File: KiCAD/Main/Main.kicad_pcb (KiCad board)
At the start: 4 copper layers, 60 x 150 mm, 99 parts, among them J1 Micro_SD_Card_Det2, J2 Screw_Terminal_01x09, J3 Screw_Terminal_01x09, J4 USB_C_Receptacle_USB2.0_16P, J5 Conn_02x04_Counter_Clockwise, J8 Conn_Coaxial, J9 Conn_Coaxial, Q1 AO3400A, Q2 AO3400A, Q3 AO3400A, Q4 2N7002, SW1 RESET, SW2 USER, U1 LM2596S-3.3, U11 BMP390L, U12 BMP390L, U13 BMP390L, U14 BMI270, U15 BMI270, U16 BMI270, U17 SHT4x, U2 TPS2121RUXR, U3 LIS2MDL, U4 STM32H750VBTx, U5 MAX-M8Q, U7 ISM6HG256x, Y2 SiT8008xx-2x-xxE (25MHz)

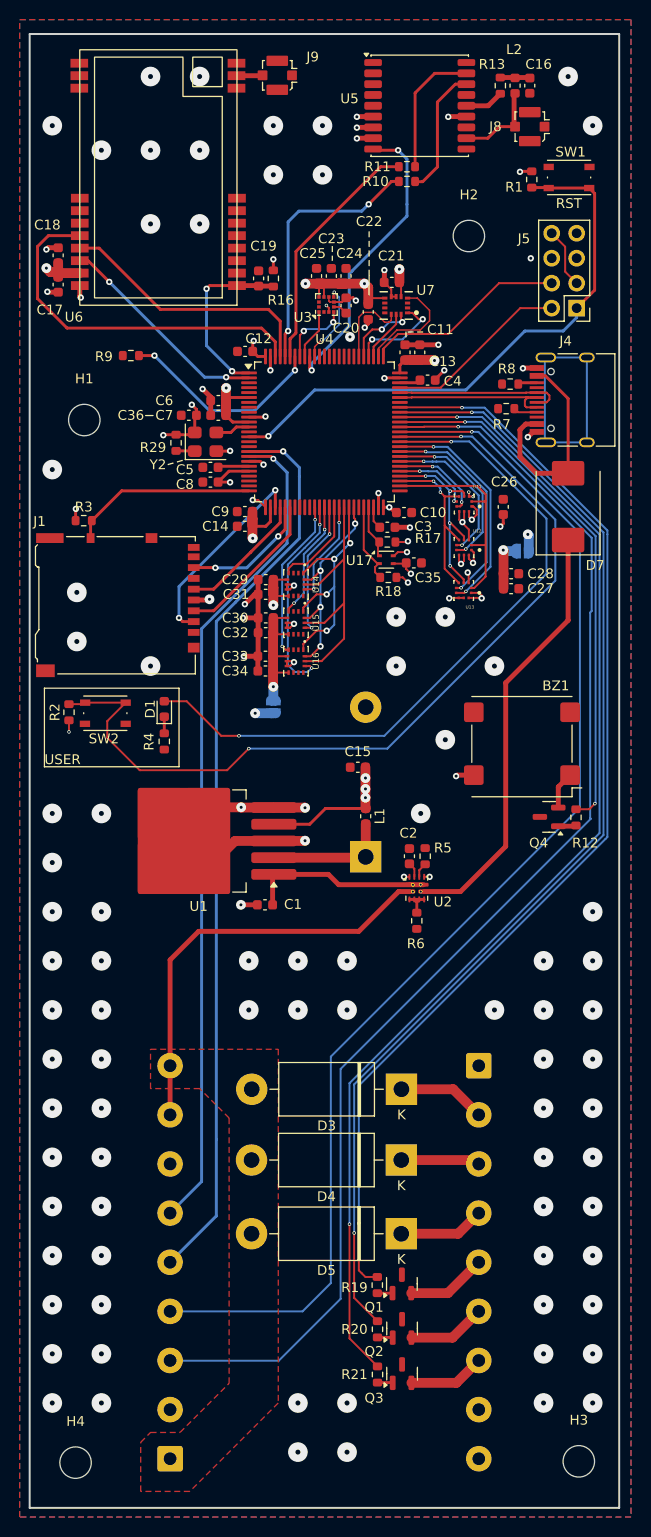
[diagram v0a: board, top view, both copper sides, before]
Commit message: Update aux magnetometer, test THs, and silkscreens
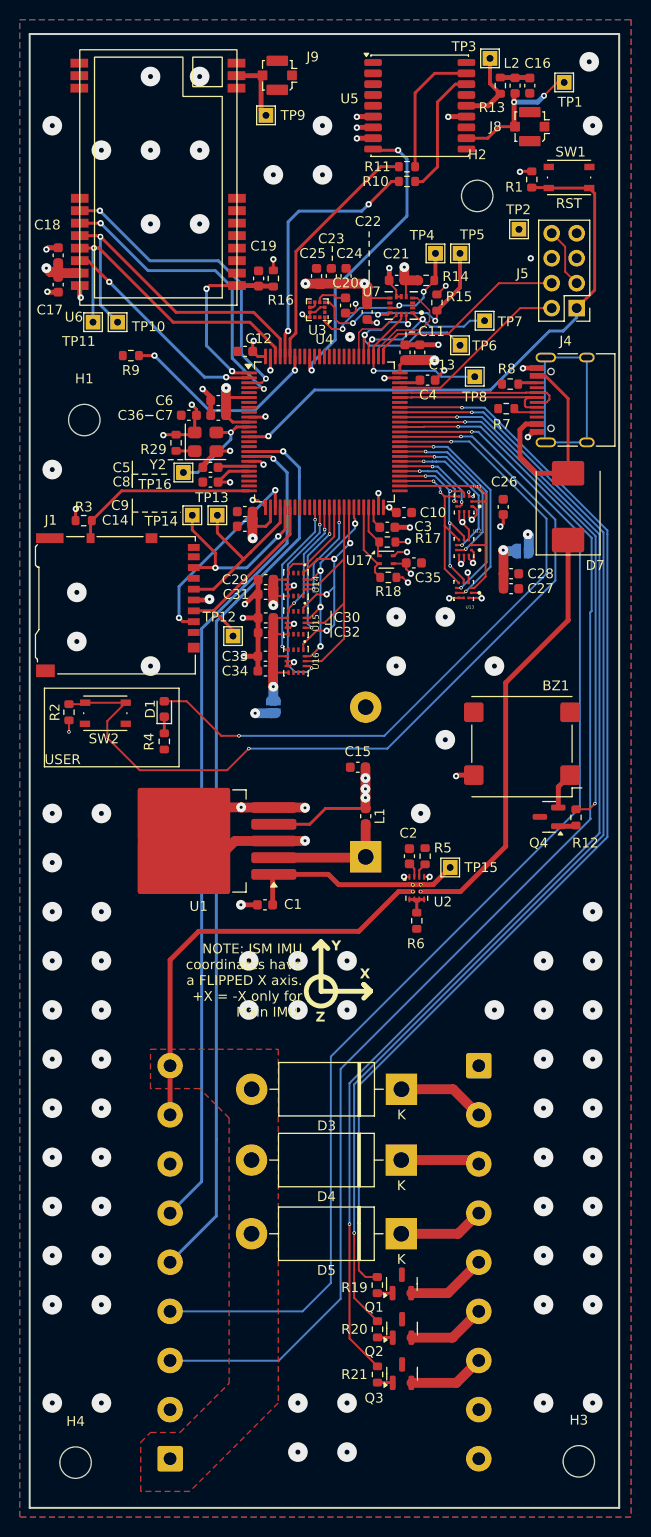
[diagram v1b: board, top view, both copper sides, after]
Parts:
- added R14: 10k, Resistor_SMD:R_0603_1608Metric, F.Cu at (148.1, 55.8)
- added R15: 10k, Resistor_SMD:R_0603_1608Metric, F.Cu at (149.2, 58.0)
- added TP1: TestPoint, TestPoint:TestPoint_THTPad_1.5x1.5mm_Drill0.7mm, F.Cu at (162.1, 35.6)
- added TP10: TestPoint, TestPoint:TestPoint_THTPad_1.5x1.5mm_Drill0.7mm, F.Cu at (116.7, 60.0)
- added TP11: TestPoint, TestPoint:TestPoint_THTPad_1.5x1.5mm_Drill0.7mm, F.Cu at (114.2, 60.0)
- added TP12: TestPoint, TestPoint:TestPoint_THTPad_1.5x1.5mm_Drill0.7mm, F.Cu at (128.4, 92.0)
- added TP13: TestPoint, TestPoint:TestPoint_THTPad_1.5x1.5mm_Drill0.7mm, F.Cu at (126.8, 79.7)
- added TP14: TestPoint, TestPoint:TestPoint_THTPad_1.5x1.5mm_Drill0.7mm, F.Cu at (124.2, 79.7)
- added TP15: TestPoint, TestPoint:TestPoint_THTPad_1.5x1.5mm_Drill0.7mm, F.Cu at (150.5, 115.5)
- added TP16: TestPoint, TestPoint:TestPoint_THTPad_1.5x1.5mm_Drill0.7mm, F.Cu at (123.3, 75.3)
- added TP2: TestPoint, TestPoint:TestPoint_THTPad_1.5x1.5mm_Drill0.7mm, F.Cu at (157.5, 50.5)
- added TP3: TestPoint, TestPoint:TestPoint_THTPad_1.5x1.5mm_Drill0.7mm, F.Cu at (154.6, 33.1)
- added TP4: TestPoint, TestPoint:TestPoint_THTPad_1.5x1.5mm_Drill0.7mm, F.Cu at (149.0, 53.0)
- added TP5: TestPoint, TestPoint:TestPoint_THTPad_1.5x1.5mm_Drill0.7mm, F.Cu at (151.5, 53.0)
- added TP6: TestPoint, TestPoint:TestPoint_THTPad_1.5x1.5mm_Drill0.7mm, F.Cu at (151.5, 62.4)
- added TP7: TestPoint, TestPoint:TestPoint_THTPad_1.5x1.5mm_Drill0.7mm, F.Cu at (154.0, 59.9)
- added TP8: TestPoint, TestPoint:TestPoint_THTPad_1.5x1.5mm_Drill0.7mm, F.Cu at (153.0, 65.5)
- added TP9: TestPoint, TestPoint:TestPoint_THTPad_1.5x1.5mm_Drill0.7mm, F.Cu at (131.8, 39.0)
- moved H2 4.17 mm to (153.2, 47.1)
- moved U3 1.07 mm to (137.0, 58.7), turned to 180 degrees
- moved C21 0.54 mm to (145.1, 55.7)
- moved U7 0.52 mm to (145.5, 58.3)
- moved C22 0.11 mm to (142.1, 59.0)
- moved C20 0.05 mm to (139.8, 58.3), turned to -90 degrees
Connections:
- U3 pad 1: /IMUs/SCL_LIS -> Net-(U3-SCL/SPC)
- U3 pad 4: /IMUs/SDA_LIS -> Net-(U3-SDA/SDI/SDO)
- U3 pad 7: /IMUs/INT_LIS -> unconnected-(U3-DRDY-Pad7)
- U4 pad 3: unconnected-(U4-PE4-Pad3) -> /Microcontroller/M0_Radio
- U4 pad 4: unconnected-(U4-PE5-Pad4) -> /Microcontroller/M1_Radio
- U4 pad 90: /IMUs/INT_LIS -> unconnected-(U4-PB4-Pad90)
- U4 pad 92: /IMUs/SCL_LIS -> unconnected-(U4-PB6-Pad92)
- U4 pad 93: /IMUs/SDA_LIS -> unconnected-(U4-PB7-Pad93)
- U4 pad 97: /Microcontroller/Radio RX -> /Microcontroller/Radio TX
- U4 pad 98: /Microcontroller/Radio TX -> /Microcontroller/Radio RX
- U6 pad 20: GND -> /Microcontroller/M0_Radio
- U6 pad 21: GND -> /Microcontroller/M1_Radio
- U7 pad 10: unconnected-(U7-OCS_Aux-Pad10) -> Net-(U3-SCL/SPC)
- U7 pad 11: unconnected-(U7-SDO_Aux-Pad11) -> Net-(U3-SDA/SDI/SDO)
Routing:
- net /Microcontroller/M0_Radio: track 0.00 -> 32.1 mm, vias 0 -> 2
- net /Microcontroller/M1_Radio: track 0.00 -> 31.5 mm, vias 0 -> 2
- net Net-(U3-SDA/SDI/SDO): track 0.00 -> 22.9 mm, vias 0 -> 3
- net Net-(U3-SCL/SPC): track 0.00 -> 18.7 mm, vias 0 -> 3
- net /IMUs/ISM_MOSI: track 7.33 -> 19.9 mm
- net /IMUs/ISM_SCK: track 5.24 -> 17.5 mm, vias 0 -> 1
- net /IMUs/INT_LIS: track 8.44 -> 0.00 mm, vias 2 -> 0
- net /IMUs/SDA_LIS: track 7.19 -> 0.00 mm, vias 2 -> 0
- net /Microcontroller/~{OSC_OUT}: track 3.56 -> 10.5 mm, vias 0 -> 1
- net /IMUs/ISM_MISO: track 9.69 -> 16.0 mm
- net /Microcontroller/SD_MISO: track 13.2 -> 19.5 mm
- net Net-(J8-In): track 8.91 -> 14.8 mm, vias 0 -> 2
- net /Microcontroller/Radio RX: track 27.1 -> 32.6 mm, vias 0 -> 1
- net /Microcontroller/SD_CLK: track 13.2 -> 18.4 mm
- net /IMUs/SCL_LIS: track 5.13 -> 0.00 mm
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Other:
- board text added: "9-Radio RF 10-Radio RX 11-Radio TX 12-SD MOSI 13-SD SCK 14-SD MISO 15-TPS Pwr-Out 16-MCU OSC-Out"
- board text added: "NOTE: ISM IMU coordinates have a FLIPPED X axis. +X = -X only for Main IMU."
- board text added: "Testing Point Legend 1-GPS RF 2-3V3 3-GPS VCC-RF 4-LIS SCL 5-LIS SDA 6-ISM MOSI 7-ISM MISO 8-ISM SCK"
- board text added: "X"
- board text added: "Y"
- board text added: "Z"

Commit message: Replace independent magnetometer, reformat test points, generate test gerber and BOM
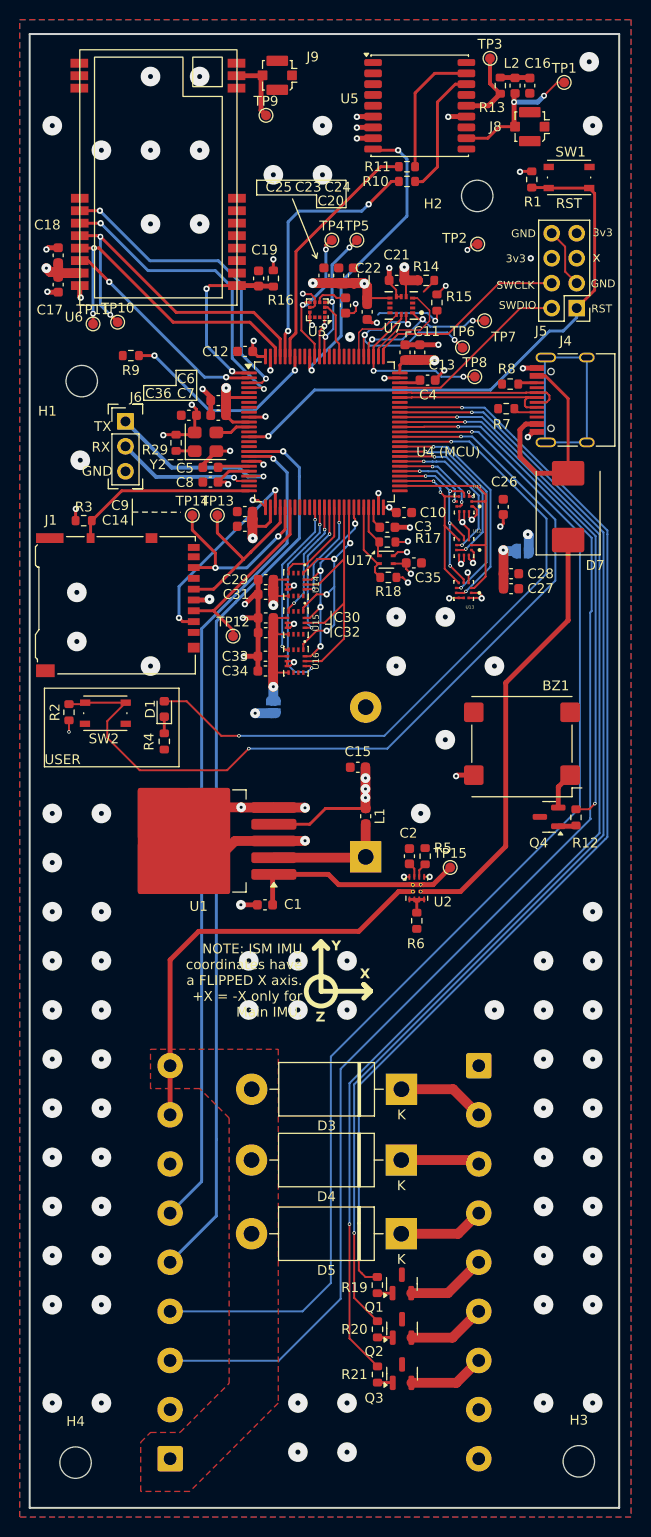
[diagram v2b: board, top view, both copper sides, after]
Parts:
- removed TP16: TestPoint, TestPoint:TestPoint_THTPad_1.5x1.5mm_Drill0.7mm
- added J6: Conn_01x03, Connector_PinHeader_2.54mm:PinHeader_1x03_P2.54mm_Vertical, F.Cu at (117.5, 70.1)
- TP1, TP10, TP11, TP12, TP13, TP14, TP15, TP2, TP3, TP4, TP5, TP6, TP7, TP8, TP9: footprint TestPoint:TestPoint_THTPad_1.5x1.5mm_Drill0.7mm -> TestPoint:TestPoint_Pad_D1.0mm
- U4 (MCU): renamed from U4
- moved TP4 10.6 mm to (138.4, 51.6)
- moved TP5 10.6 mm to (141.0, 51.6)
- moved TP2 4.46 mm to (153.3, 52.0)
- moved H1 3.97 mm to (113.0, 66.0)
- moved C23 0.75 mm to (139.2, 55.2)
- moved C24 0.75 mm to (140.7, 55.2)
- moved C25 0.75 mm to (137.7, 55.2)
- moved TP6 0.35 mm to (151.8, 62.6)
- moved TP11 0.17 mm to (114.2, 60.2)
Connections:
- TP4 pad 1: Net-(U3-SCL/SPC) -> /IMUs/MISO-Magnetometer
- TP5 pad 1: Net-(U3-SDA/SDI/SDO) -> /IMUs/MOSI-Magnetometer
- U3 pad 1: Net-(U3-SCL/SPC) -> /IMUs/SCK-Magnetometer
- U3 pad 3: +3V3 -> /IMUs/CS-Magnetometer
- U3 pad 4: Net-(U3-SDA/SDI/SDO) -> /IMUs/MOSI-Magnetometer
- U3 pad 7: unconnected-(U3-DRDY-Pad7) -> /IMUs/MISO-Magnetometer
- U4 (MCU) pad 22: unconnected-(U4-PA0-Pad22) -> /Microcontroller/UART4_TX
- U4 (MCU) pad 23: unconnected-(U4-PA1-Pad23) -> /Microcontroller/UART4_RX
- U4 (MCU) pad 85: unconnected-(U4-PD4-Pad85) -> /IMUs/CS-Magnetometer
- U4 (MCU) pad 88: unconnected-(U4-PD7-Pad88) -> /IMUs/MOSI-Magnetometer
- U4 (MCU) pad 89: unconnected-(U4-PB3-Pad89) -> /IMUs/SCK-Magnetometer
- U4 (MCU) pad 90: unconnected-(U4-PB4-Pad90) -> /IMUs/MISO-Magnetometer
- U7 pad 10: Net-(U3-SCL/SPC) -> unconnected-(U7-OCS_Aux-Pad10)
- U7 pad 11: Net-(U3-SDA/SDI/SDO) -> unconnected-(U7-SDO_Aux-Pad11)
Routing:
- net /Microcontroller/UART4_TX: track 0.00 -> 17.9 mm, vias 0 -> 1
- net Net-(U3-SCL/SPC): track 18.7 -> 1.90 mm, vias 3 -> 0
- net Net-(U3-SDA/SDI/SDO): track 22.9 -> 7.38 mm, vias 3 -> 1
- net /IMUs/MISO-Magnetometer: track 0.00 -> 14.8 mm, vias 0 -> 2
- net /Microcontroller/UART4_RX: track 0.00 -> 14.1 mm, vias 0 -> 1
- net /IMUs/MOSI-Magnetometer: track 0.00 -> 14.1 mm, vias 0 -> 3
- net /Microcontroller/~{OSC_OUT}: track 10.5 -> 3.56 mm, vias 1 -> 0
- net /IMUs/CS-Magnetometer: track 0.00 -> 5.78 mm
- net /IMUs/SCK-Magnetometer: track 0.00 -> 4.23 mm, vias 0 -> 1
- net GND: track 97.1 -> 99.0 mm, vias 115 -> 116
- net /IMUs/ISM_MOSI: track 19.9 -> 20.3 mm, vias 2 -> 3
- net +3V3: track 116.4 -> 116.7 mm, vias 36 -> 37
- net /IMUs/ISM_MISO: vias 2 -> 3
- net /Microcontroller/Radio TX: vias 1 -> 2
- net /Microcontroller/Radio RX: vias 1 -> 2
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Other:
- board text added: "3v3"
- board text added: "9-Radio RF 10-Radio RX 11-Radio TX 12-SD MOSI 13-SD SCK 14-SD MISO 15-TPS Pwr-Out"
- board text added: "GND"
- board text added: "RX"
- board text added: "SWCLK"
- board text added: "SWDIO"
- board text added: "TX"
- board text added: "Testing Point Legend 1-GPS RF 2-3V3 3-GPS VCC-RF 4-LIS MISO 5-LIS MOSI 6-ISM MOSI 7-ISM MISO 8-ISM SCK"
- board text added: "x"
- board text removed: "9-Radio RF 10-Radio RX 11-Radio TX 12-SD MOSI 13-SD SCK 14-SD MISO 15-TPS Pwr-Out 16-MCU OSC-Out"
- board text removed: "Testing Point Legend 1-GPS RF 2-3V3 3-GPS VCC-RF 4-LIS SCL 5-LIS SDA 6-ISM MOSI 7-ISM MISO 8-ISM SCK"

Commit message: Update BOM and respective components according to LCSC supply, remove previously generated production files
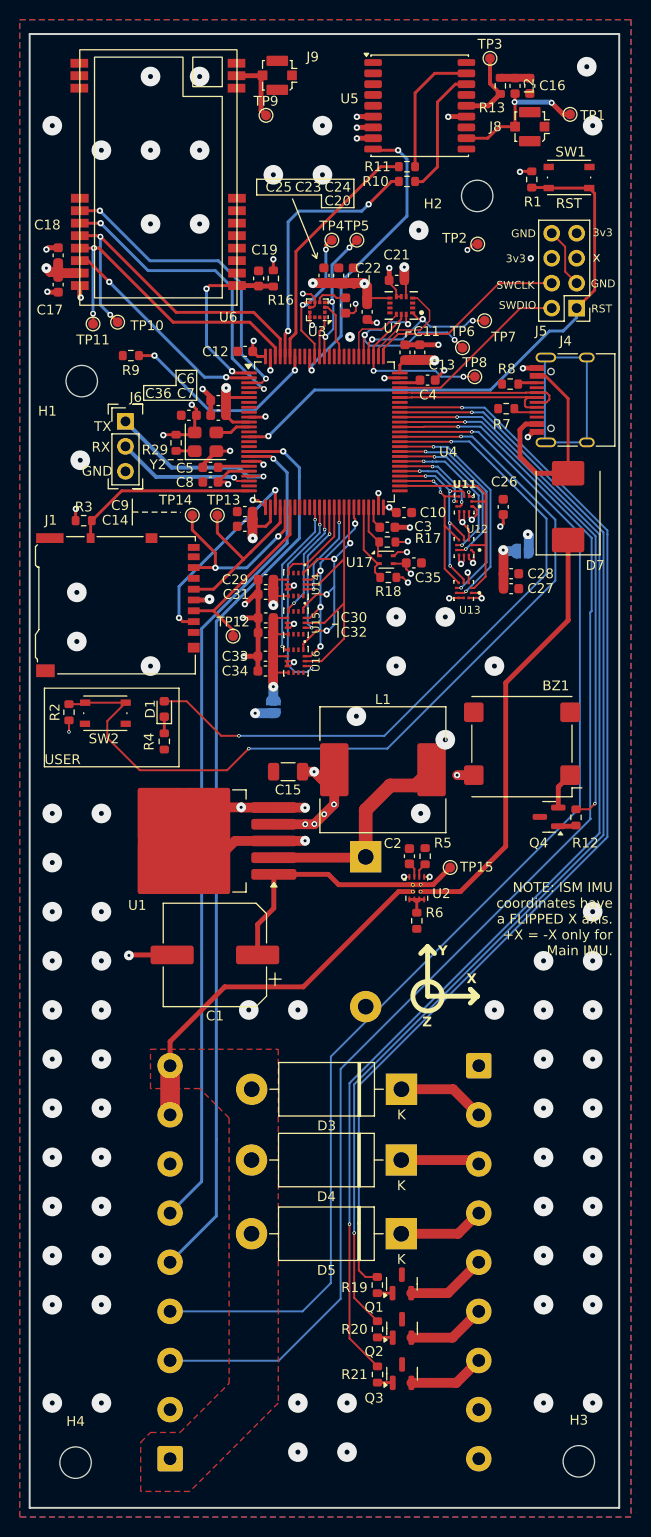
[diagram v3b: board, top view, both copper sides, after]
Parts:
- removed R14, R15: 10k, Resistor_SMD:R_0603_1608Metric
- C1: footprint Capacitor_SMD:C_0603_1608Metric -> Capacitor_SMD:CP_Elec_10x12.6
- C15: footprint Capacitor_SMD:C_0603_1608Metric -> Capacitor_SMD:C_1206_3216Metric
- L1: footprint Inductor_SMD:L_0603_1608Metric -> Inductor_SMD:L_SXN_SMDRI127
- U4: renamed from U4 (MCU)
- moved C1 7.21 mm to (126.5, 124.4), turned to 180 degrees
- moved C15 7.11 mm to (134.0, 105.8)
- moved L1 5.04 mm to (143.7, 105.5), turned to 0 degrees
- moved TP1 3.30 mm to (162.7, 38.9)
- turned D2 to -90 degrees
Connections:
- C1 pad 1: GND -> Net-(U1-VIN)
- C1 pad 2: Net-(U1-VIN) -> GND
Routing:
- net Net-(D2-K): track 12.7 -> 22.6 mm
- net Net-(U3-SDA/SDI/SDO): track 7.38 -> 0.00 mm, vias 1 -> 0
- net Net-(U1-VIN): track 22.3 -> 28.0 mm
- net Net-(D3-A): track 43.1 -> 38.2 mm
- net +3V3: track 116.7 -> 113.5 mm, vias 37 -> 38
- net GND: track 99.0 -> 101.7 mm, vias 116 -> 114
- net Net-(U3-SCL/SPC): track 1.90 -> 0.00 mm
- net /IMUs/SCK-Magnetometer: vias 1 -> 0
